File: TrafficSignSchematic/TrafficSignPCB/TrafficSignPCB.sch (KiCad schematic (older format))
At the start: 29 parts, among them J1 IDC connector, J2 3.96mm pitch 4-pin polarized 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, J3 Power In, U1 ATmega328P-PU, U2 SIM800L, Y1 16MHz

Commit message: Added PCB and schematic images
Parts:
- R6: footprint (none) -> Resistor_THT:R_Axial_DIN0204_L3.6mm_D1.6mm_P7.62mm_Horizontal
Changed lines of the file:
@@
 F 0 "R6" V 3700 2700 50  0000 C CNN
 F 1 "10k" V 3700 2500 50  0000 C CNN
-F 2 "" V 3730 2600 50  0001 C CNN
+F 2 "Resistor_THT:R_Axial_DIN0204_L3.6mm_D1.6mm_P7.62mm_Horizontal" V 3730 2600 50  0001 C CNN
 F 3 "~" H 3800 2600 50  0001 C CNN
 	1    3800 2600

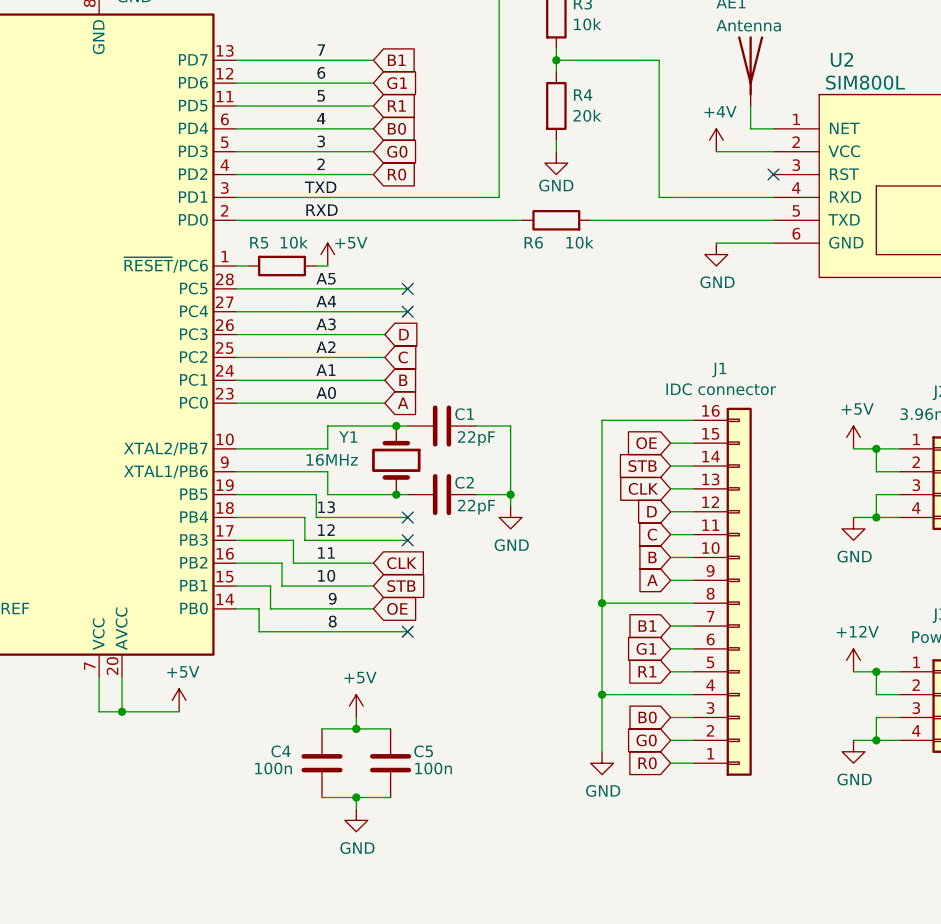
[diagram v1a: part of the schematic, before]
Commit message: Changed buck converter layout
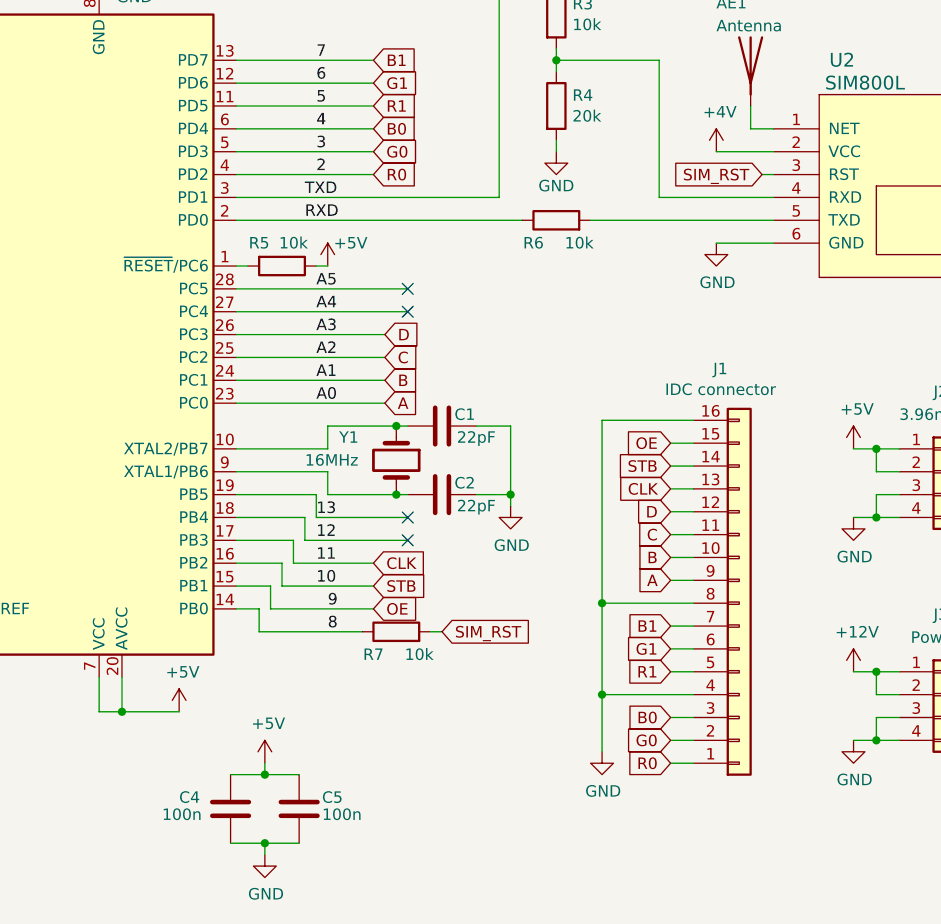
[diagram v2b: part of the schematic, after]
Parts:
- added R7: 10k, Resistor_THT:R_Axial_DIN0204_L3.6mm_D1.6mm_P7.62mm_Horizontal, symbol Device:R
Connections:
- net 8: now also R7.1
- net SIM_RST: now reaches U2.3 (RST)
- net SIM_RST: now also R7.2
- no-connect marks 12 -> 10
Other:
- moved on the sheet: C4, C5
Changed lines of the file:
@@
 Wire Wire Line
 	4650 2200 4750 2200
-NoConn ~ 4750 2400
 Wire Wire Line
 	4250 2500 4750 2500
@@
 Wire Wire Line
 	3450 3800 3600 3800
-NoConn ~ 3150 4400
 NoConn ~ 3150 4000
 NoConn ~ 3150 3900
@@
 R0
 Wire Wire Line
-	2500 4400 3150 4400
+	2500 4400 2950 4400
 Wire Wire Line
 	2500 4300 2500 4400
@@
 L power:+5V #PWR0122
 U 1 1 5E5ABDC2
-P 2925 4775
-F 0 "#PWR0122" H 2925 4625 50  0001 C CNN
-F 1 "+5V" H 2940 4948 50  0000 C CNN
-F 2 "" H 2925 4775 50  0001 C CNN
-F 3 "" H 2925 4775 50  0001 C CNN
-	1    2925 4775
+P 2525 4975
+F 0 "#PWR0122" H 2525 4825 50  0001 C CNN
+F 1 "+5V" H 2540 5148 50  0000 C CNN
+F 2 "" H 2525 4975 50  0001 C CNN
+F 3 "" H 2525 4975 50  0001 C CNN
+	1    2525 4975
 	1    0    0    -1
 $EndComp
@@
 L power:GND #PWR0123
 U 1 1 5E5B557C
-P 2925 5175
-F 0 "#PWR0123" H 2925 4925 50  0001 C CNN
-F 1 "GND" H 2930 5002 50  0000 C CNN
-F 2 "" H 2925 5175 50  0001 C CNN
-F 3 "" H 2925 5175 50  0001 C CNN
-	1    2925 5175
+P 2525 5375
+F 0 "#PWR0123" H 2525 5125 50  0001 C CNN
+F 1 "GND" H 2530 5202 50  0000 C CNN
+F 2 "" H 2525 5375 50  0001 C CNN
+F 3 "" H 2525 5375 50  0001 C CNN
+	1    2525 5375
 	1    0    0    -1
 $EndComp
@@
 L Device:C C4
 U 1 1 5E5BEE3A
-P 2775 4975
-F 0 "C4" H 2550 5025 50  0000 L CNN
-F 1 "100n" H 2475 4950 50  0000 L CNN
-F 2 "Capacitor_THT:C_Disc_D4.3mm_W1.9mm_P5.00mm" H 2813 4825 50  0001 C CNN
-F 3 "https://store.comet.bg/Catalogue/Product/5920/" H 2775 4975 50  0001 C CNN
-	1    2775 4975
+P 2375 5175
+F 0 "C4" H 2150 5225 50  0000 L CNN
+F 1 "100n" H 2075 5150 50  0000 L CNN
+F 2 "Capacitor_THT:C_Disc_D4.3mm_W1.9mm_P5.00mm" H 2413 5025 50  0001 C CNN
+F 3 "https://store.comet.bg/Catalogue/Product/5920/" H 2375 5175 50  0001 C CNN
+	1    2375 5175
 	1    0    0    -1
 $EndComp
@@
 L Device:C C5
 U 1 1 5E5C89EE
-P 3075 4975
-F 0 "C5" H 3175 5025 50  0000 L CNN
-F 1 "100n" H 3175 4950 50  0000 L CNN
-F 2 "Capacitor_THT:C_Disc_D4.3mm_W1.9mm_P5.00mm" H 3113 4825 50  0001 C CNN
-F 3 "https://store.comet.bg/Catalogue/Product/5920/" H 3075 4975 50  0001 C CNN
-	1    3075 4975
-	1    0    0    -1
-$EndComp
-Wire Wire Line
-	2775 4825 2925 4825
-Wire Wire Line
-	2925 4775 2925 4825
-Connection ~ 2925 4825
-Wire Wire Line
-	2925 4825 3075 4825
-Wire Wire Line
-	2775 5125 2925 5125
-Wire Wire Line
-	2925 5175 2925 5125
-Connection ~ 2925 5125
-Wire Wire Line
-	2925 5125 3075 5125
+P 2675 5175
+F 0 "C5" H 2775 5225 50  0000 L CNN
+F 1 "100n" H 2775 5150 50  0000 L CNN
+F 2 "Capacitor_THT:C_Disc_D4.3mm_W1.9mm_P5.00mm" H 2713 5025 50  0001 C CNN
+F 3 "https://store.comet.bg/Catalogue/Product/5920/" H 2675 5175 50  0001 C CNN
+	1    2675 5175
+	1    0    0    -1
+$EndComp
+Wire Wire Line
+	2375 5025 2525 5025
+Wire Wire Line
+	2525 4975 2525 5025
+Connection ~ 2525 5025
+Wire Wire Line
+	2525 5025 2675 5025
+Wire Wire Line
+	2375 5325 2525 5325
+Wire Wire Line
+	2525 5375 2525 5325
+Connection ~ 2525 5325
+Wire Wire Line
+	2525 5325 2675 5325
 $Comp
 L Device:R R6
@@
 Wire Wire Line
 	3950 2600 4750 2600
+$Comp
+L Device:R R7
+U 1 1 5E295091
+P 3100 4400
+F 0 "R7" V 3000 4500 50  0000 C CNN
+F 1 "10k" V 3000 4300 50  0000 C CNN
+F 2 "Resistor_THT:R_Axial_DIN0204_L3.6mm_D1.6mm_P7.62mm_Horizontal" V 3030 4400 50  0001 C CNN
+F 3 "~" H 3100 4400 50  0001 C CNN
+	1    3100 4400
+	0    -1   -1   0
+$EndComp
+Wire Wire Line
+	3250 4400 3300 4400
+Wire Wire Line
+	4750 2400 4700 2400
+Text GLabel 4700 2400 0    50   Input ~ 0
+SIM_RST
+Text GLabel 3300 4400 2    50   Input ~ 0
+SIM_RST
 $EndSCHEMATC
